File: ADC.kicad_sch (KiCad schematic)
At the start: 43 parts, among them U1 MCP3008

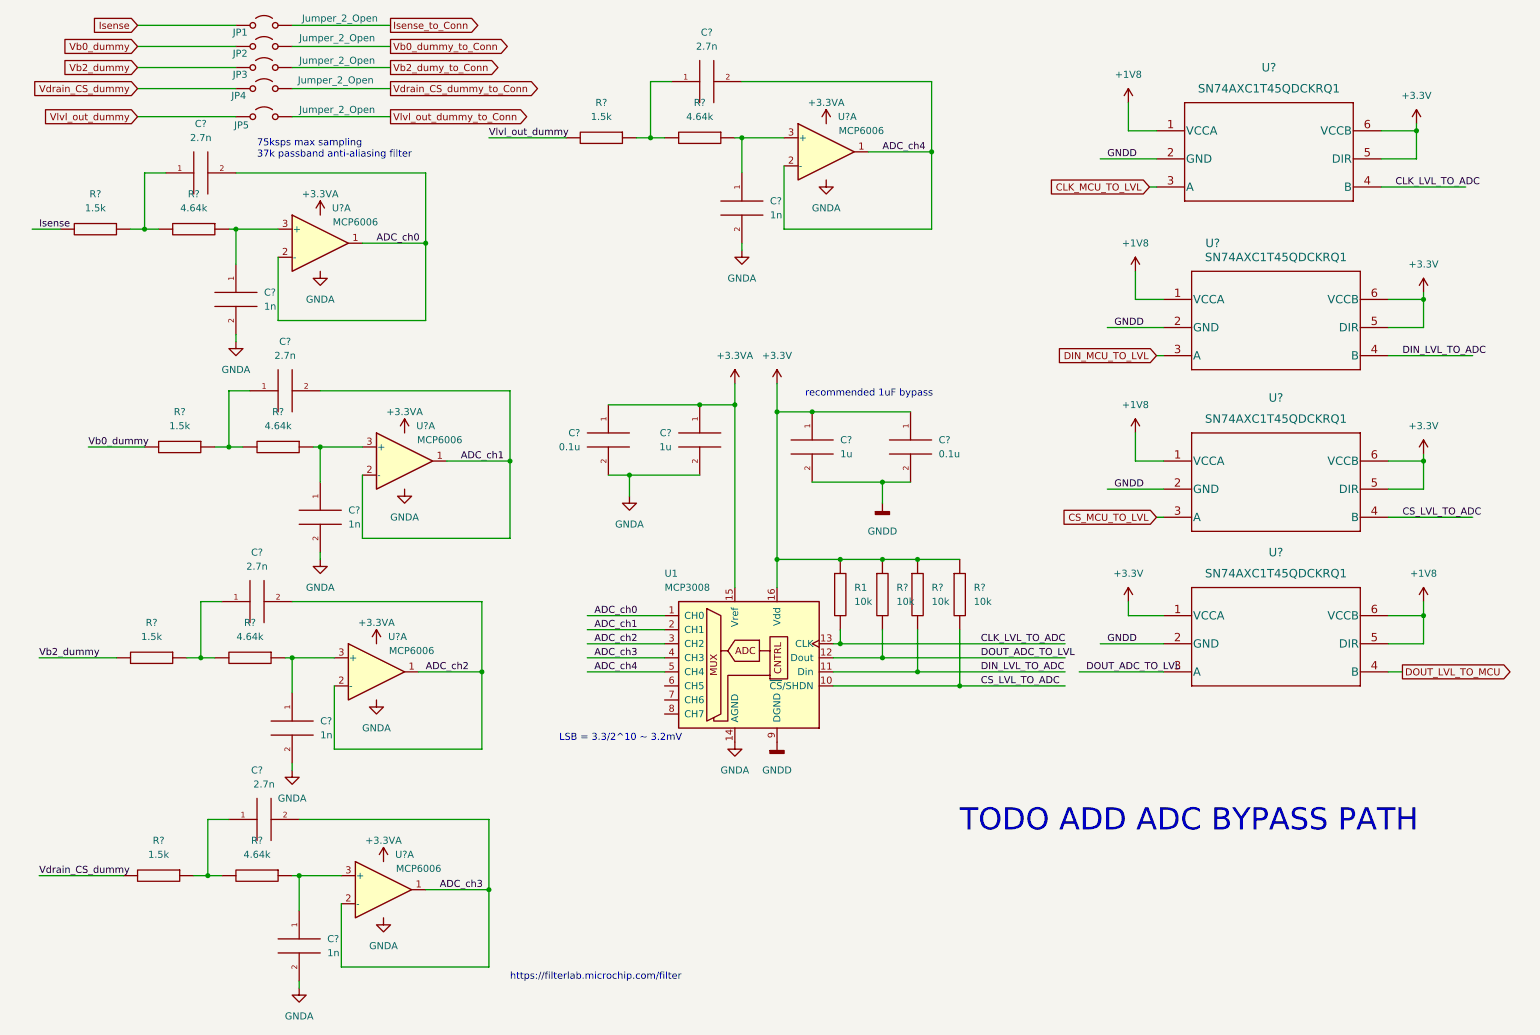
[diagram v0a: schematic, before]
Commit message: ADC swap for multi-channel opamp
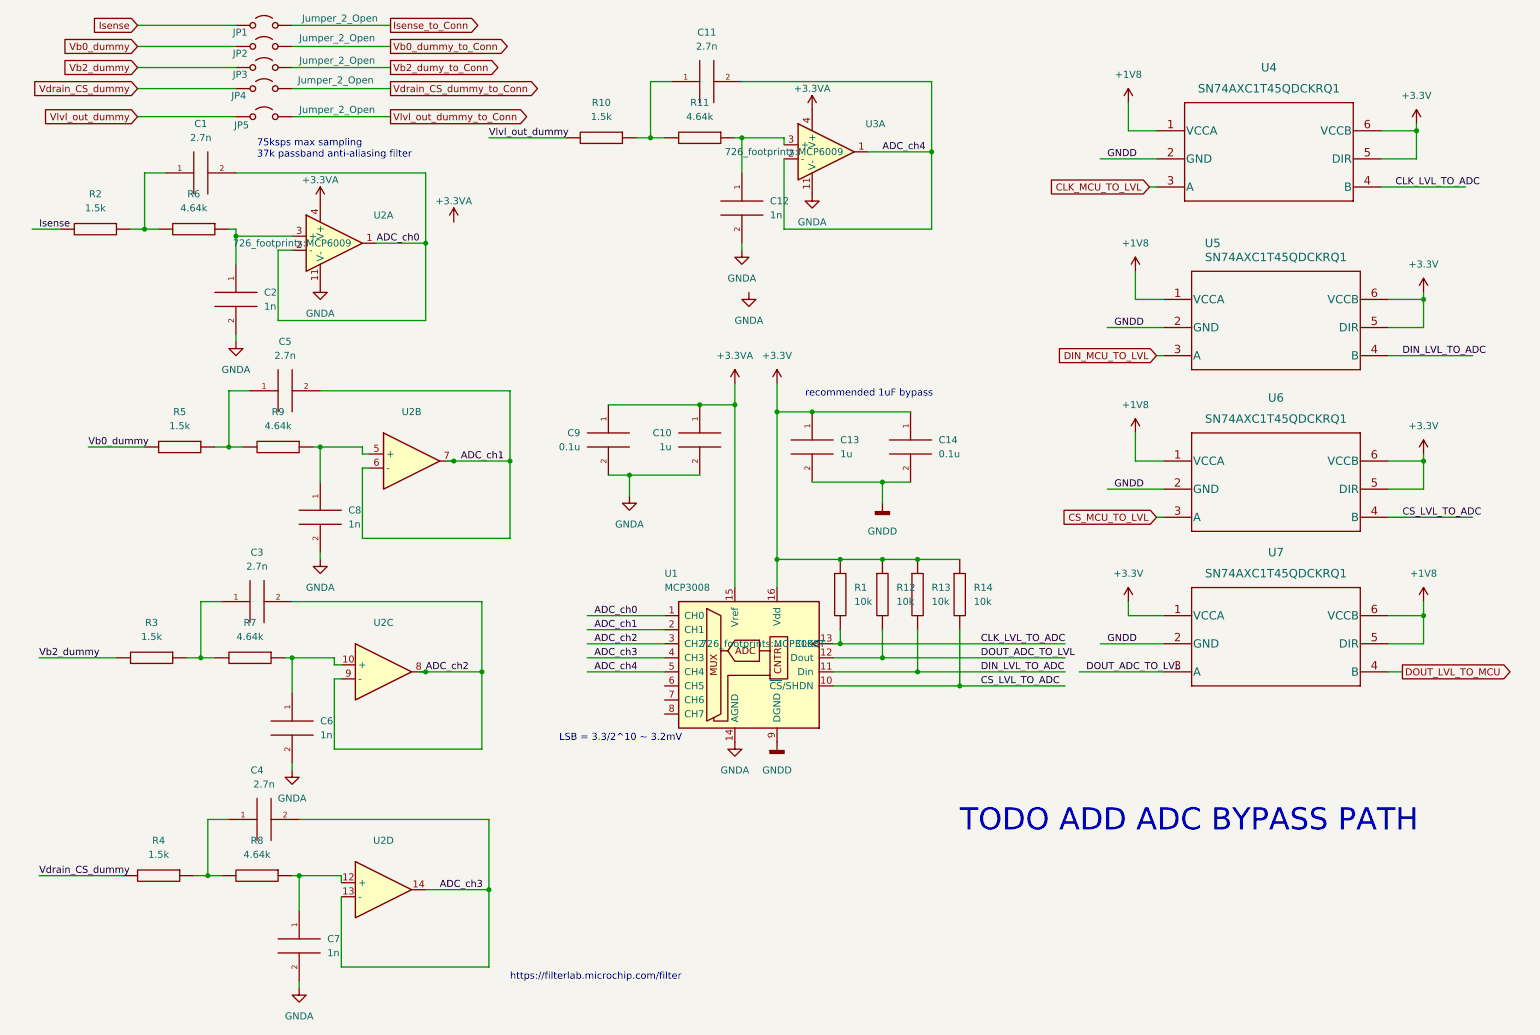
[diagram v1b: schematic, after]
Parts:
- removed U? (x5): MCP6006, symbol ISense:MCP6006
- added U2, U3: ~, 726_footprints:MCP6009, symbol MCP6009:MCP6009_multiUnit
- U1: footprint (none) -> 726_footprints:MCP3008T
- gave numbers to parts that had none: 31
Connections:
- net +3.3VA: now also U2.4 (V+), U3.4 (V+)
- net ADC_ch0: now also U2.1, U2.2 (-)
- net ADC_ch1: now also U2.6 (-), U2.7
- net ADC_ch2: now also U2.8, U2.9 (-)
- net ADC_ch3: now also U2.13 (-), U2.14
- net ADC_ch4: now also U3.1, U3.2 (-)
- net GNDA: now also U2.11 (V-), U3.11 (V-)
- net at C8.1, R9.1: now also U2.5 (+)
- net at C7.1, R8.1: now also U2.12 (+)
- net at C2.1, R6.1: now also U2.3 (+)
- net at C12.1, R11.1: now also U3.3 (+)
- net at C6.1, R7.1: now also U2.10 (+)
